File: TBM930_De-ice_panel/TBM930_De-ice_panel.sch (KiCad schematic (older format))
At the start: 77 parts, among them J1 SW_AIRFRAME_DE_ICE, J10 AVR-ISP-6, J11 Screw_Terminal_01x02, J2 SW_ICE_LIGHT, J3 SW_PROP_DE_ICE, J4 SW_WIND_SHIELD, J5 SW_PITOT_L_HTR, J6 SW_PITOT_R_HTR, J7 SW_INERT_SEP, J8 Barrel_Jack, J9 USB_B_Mini, SW1 SW_Push, SW2 SW_Push, U1 TLC5917IN, U2 TLC5917IN, U3 ATmega32U4-MU, Y1 Crystal_GND24

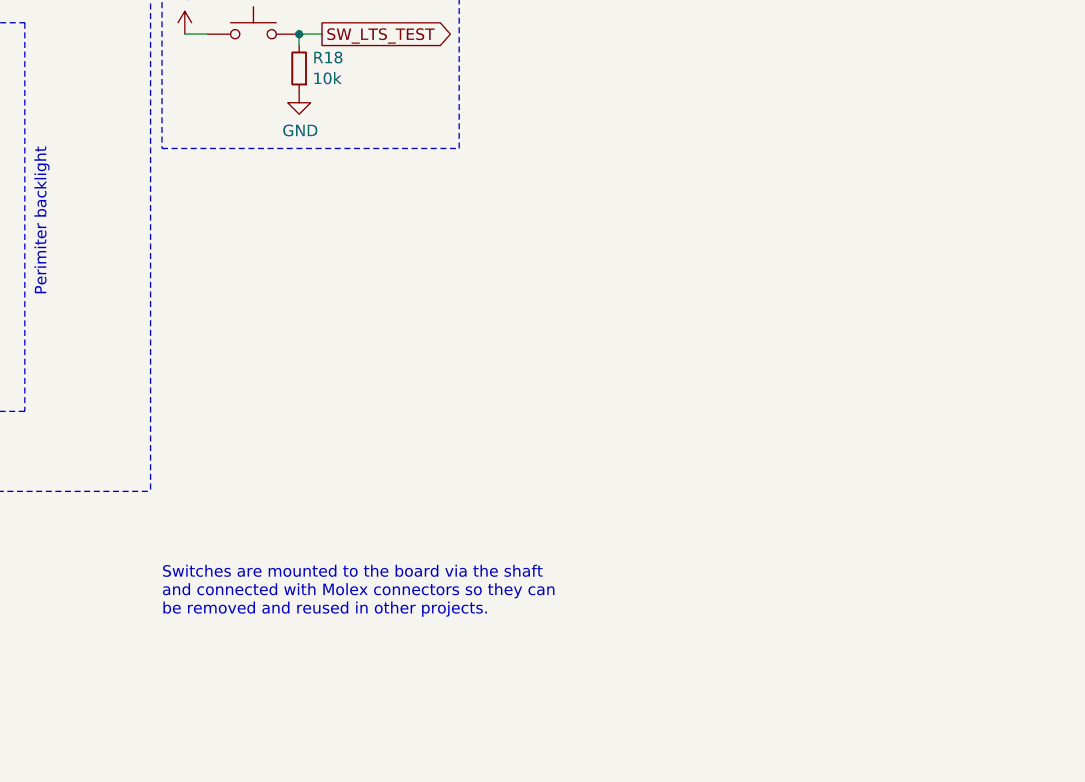
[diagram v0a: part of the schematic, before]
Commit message: Fix PCB holes
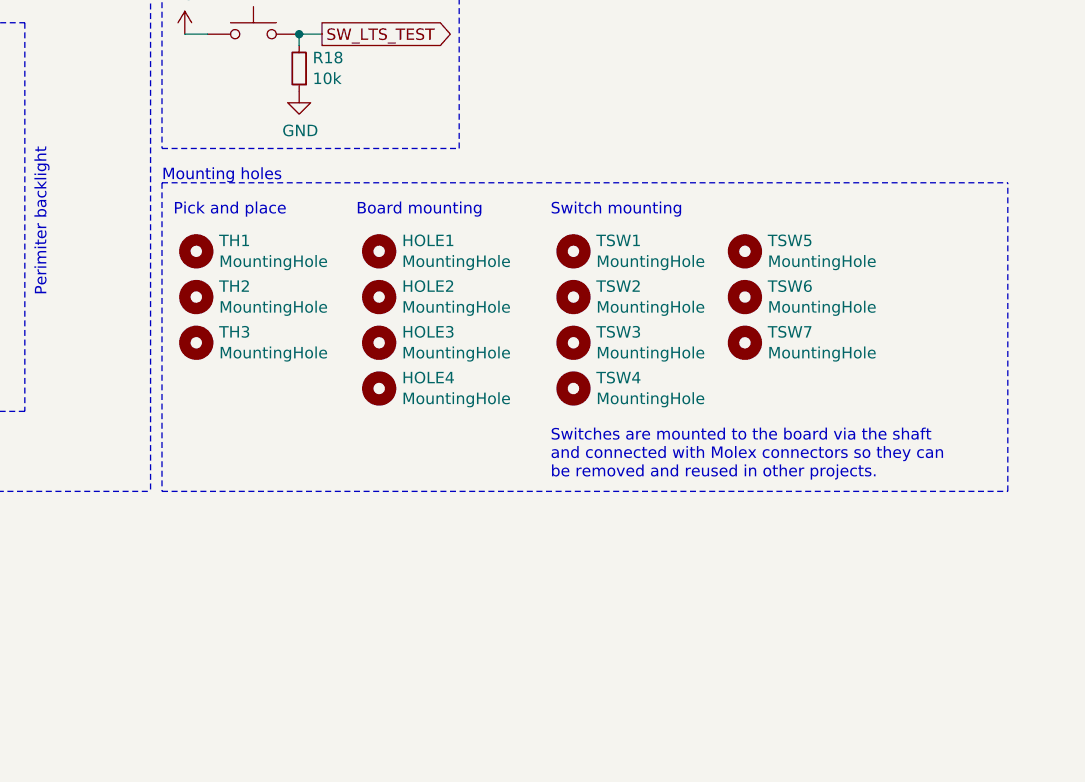
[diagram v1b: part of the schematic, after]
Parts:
- added HOLE1, HOLE2, HOLE3, HOLE4: MountingHole, MountingHole:MountingHole_3.2mm_M3, symbol Mechanical:MountingHole
- added TH1, TH2, TH3: MountingHole, TBM930 - De-ice panel:JLCPCB_Tooling_Hole, symbol Mechanical:MountingHole
- added TSW1, TSW2, TSW3, TSW4, TSW5, TSW6, TSW7: MountingHole, TBM930 - De-ice panel:MiniToggleSPDT_screw_mount, symbol Mechanical:MountingHole
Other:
- note added: "Board mounting"
- note added: "Mounting holes"
- note added: "Pick and place"
- note added: "Switch mounting"
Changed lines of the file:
@@
 	1    0    0    -1
 $EndComp
-Text Notes 9150 6350 0    50   ~ 0
+Text Notes 10850 5750 0    50   ~ 0
 Switches are mounted to the board via the shaft\nand connected with Molex connectors so they can\nbe removed and reused in other projects.\n
 Text GLabel 7000 2450 0    50   Input ~ 0
@@
 F 1 "AVR-ISP-6" H 3521 6855 50  0000 R CNN
 F 2 "Connector_PinHeader_2.54mm:PinHeader_2x03_P2.54mm_Vertical" V 3600 6900 50  0001 C CNN
-F 3 " ~" H 2575 6300 50  0001 C CNN
+F 3 "~" H 2575 6300 50  0001 C CNN
 	1    3850 6850
 	1    0    0    -1
@@
 	-1   0    0    1
 $EndComp
+$Comp
+L Mechanical:MountingHole TH1
+U 1 1 61445600
+P 9300 4750
+F 0 "TH1" H 9400 4796 50  0000 L CNN
+F 1 "MountingHole" H 9400 4705 50  0000 L CNN
+F 2 "TBM930 - De-ice panel:JLCPCB_Tooling_Hole" H 9300 4750 50  0001 C CNN
+F 3 "~" H 9300 4750 50  0001 C CNN
+	1    9300 4750
+	1    0    0    -1
+$EndComp
+$Comp
+L Mechanical:MountingHole TH2
+U 1 1 61446718
+P 9300 4950
+F 0 "TH2" H 9400 4996 50  0000 L CNN
+F 1 "MountingHole" H 9400 4905 50  0000 L CNN
+F 2 "TBM930 - De-ice panel:JLCPCB_Tooling_Hole" H 9300 4950 50  0001 C CNN
+F 3 "~" H 9300 4950 50  0001 C CNN
+	1    9300 4950
+	1    0    0    -1
+$EndComp
+$Comp
+L Mechanical:MountingHole TH3
+U 1 1 6145058F
+P 9300 5150
+F 0 "TH3" H 9400 5196 50  0000 L CNN
+F 1 "MountingHole" H 9400 5105 50  0000 L CNN
+F 2 "TBM930 - De-ice panel:JLCPCB_Tooling_Hole" H 9300 5150 50  0001 C CNN
+F 3 "~" H 9300 5150 50  0001 C CNN
+	1    9300 5150
+	1    0    0    -1
+$EndComp
+$Comp
+L Mechanical:MountingHole HOLE1
+U 1 1 6145AC3B
+P 10100 4750
+F 0 "HOLE1" H 10200 4796 50  0000 L CNN
+F 1 "MountingHole" H 10200 4705 50  0000 L CNN
+F 2 "MountingHole:MountingHole_3.2mm_M3" H 10100 4750 50  0001 C CNN
+F 3 "~" H 10100 4750 50  0001 C CNN
+	1    10100 4750
+	1    0    0    -1
+$EndComp
+$Comp
+L Mechanical:MountingHole HOLE2
+U 1 1 6146567E
+P 10100 4950
+F 0 "HOLE2" H 10200 4996 50  0000 L CNN
+F 1 "MountingHole" H 10200 4905 50  0000 L CNN
+F 2 "MountingHole:MountingHole_3.2mm_M3" H 10100 4950 50  0001 C CNN
+F 3 "~" H 10100 4950 50  0001 C CNN
+	1    10100 4950
+	1    0    0    -1
+$EndComp
+$Comp
+L Mechanical:MountingHole HOLE3
+U 1 1 6146F39B
+P 10100 5150
+F 0 "HOLE3" H 10200 5196 50  0000 L CNN
+F 1 "MountingHole" H 10200 5105 50  0000 L CNN
+F 2 "MountingHole:MountingHole_3.2mm_M3" H 10100 5150 50  0001 C CNN
+F 3 "~" H 10100 5150 50  0001 C CNN
+	1    10100 5150
+	1    0    0    -1
+$EndComp
+$Comp
+L Mechanical:MountingHole HOLE4
+U 1 1 614794E2
+P 10100 5350
+F 0 "HOLE4" H 10200 5396 50  0000 L CNN
+F 1 "MountingHole" H 10200 5305 50  0000 L CNN
+F 2 "MountingHole:MountingHole_3.2mm_M3" H 10100 5350 50  0001 C CNN
+F 3 "~" H 10100 5350 50  0001 C CNN
+	1    10100 5350
+	1    0    0    -1
+$EndComp
+$Comp
+L Mechanical:MountingHole TSW1
+U 1 1 61491315
+P 10950 4750
+F 0 "TSW1" H 11050 4796 50  0000 L CNN
+F 1 "MountingHole" H 11050 4705 50  0000 L CNN
+F 2 "TBM930 - De-ice panel:MiniToggleSPDT_screw_mount" H 10950 4750 50  0001 C CNN
+F 3 "~" H 10950 4750 50  0001 C CNN
+	1    10950 4750
+	1    0    0    -1
+$EndComp
+$Comp
+L Mechanical:MountingHole TSW2
+U 1 1 6149AD01
+P 10950 4950
+F 0 "TSW2" H 11050 4996 50  0000 L CNN
+F 1 "MountingHole" H 11050 4905 50  0000 L CNN
+F 2 "TBM930 - De-ice panel:MiniToggleSPDT_screw_mount" H 10950 4950 50  0001 C CNN
+F 3 "~" H 10950 4950 50  0001 C CNN
+	1    10950 4950
+	1    0    0    -1
+$EndComp
+$Comp
+L Mechanical:MountingHole TSW3
+U 1 1 614A4147
+P 10950 5150
+F 0 "TSW3" H 11050 5196 50  0000 L CNN
+F 1 "MountingHole" H 11050 5105 50  0000 L CNN
+F 2 "TBM930 - De-ice panel:MiniToggleSPDT_screw_mount" H 10950 5150 50  0001 C CNN
+F 3 "~" H 10950 5150 50  0001 C CNN
+	1    10950 5150
+	1    0    0    -1
+$EndComp
+$Comp
+L Mechanical:MountingHole TSW4
+U 1 1 614AD526
+P 10950 5350
+F 0 "TSW4" H 11050 5396 50  0000 L CNN
+F 1 "MountingHole" H 11050 5305 50  0000 L CNN
+F 2 "TBM930 - De-ice panel:MiniToggleSPDT_screw_mount" H 10950 5350 50  0001 C CNN
+F 3 "~" H 10950 5350 50  0001 C CNN
+	1    10950 5350
+	1    0    0    -1
+$EndComp
+$Comp
+L Mechanical:MountingHole TSW5
+U 1 1 614B67D6
+P 11700 4750
+F 0 "TSW5" H 11800 4796 50  0000 L CNN
+F 1 "MountingHole" H 11800 4705 50  0000 L CNN
+F 2 "TBM930 - De-ice panel:MiniToggleSPDT_screw_mount" H 11700 4750 50  0001 C CNN
+F 3 "~" H 11700 4750 50  0001 C CNN
+	1    11700 4750
+	1    0    0    -1
+$EndComp
+$Comp
+L Mechanical:MountingHole TSW6
+U 1 1 614BFB8D
+P 11700 4950
+F 0 "TSW6" H 11800 4996 50  0000 L CNN
+F 1 "MountingHole" H 11800 4905 50  0000 L CNN
+F 2 "TBM930 - De-ice panel:MiniToggleSPDT_screw_mount" H 11700 4950 50  0001 C CNN
+F 3 "~" H 11700 4950 50  0001 C CNN
+	1    11700 4950
+	1    0    0    -1
+$EndComp
+$Comp
+L Mechanical:MountingHole TSW7
+U 1 1 614C8F70
+P 11700 5150
+F 0 "TSW7" H 11800 5196 50  0000 L CNN
+F 1 "MountingHole" H 11800 5105 50  0000 L CNN
+F 2 "TBM930 - De-ice panel:MiniToggleSPDT_screw_mount" H 11700 5150 50  0001 C CNN
+F 3 "~" H 11700 5150 50  0001 C CNN
+	1    11700 5150
+	1    0    0    -1
+$EndComp
+Text Notes 9200 4600 0    50   ~ 0
+Pick and place
+Text Notes 10000 4600 0    50   ~ 0
+Board mounting
+Text Notes 10850 4600 0    50   ~ 0
+Switch mounting
+Wire Notes Line
+	9150 4450 9150 5800
+Wire Notes Line
+	9150 5800 12850 5800
+Wire Notes Line
+	12850 5800 12850 4450
+Wire Notes Line
+	9150 4450 12850 4450
+Text Notes 9150 4450 0    50   ~ 0
+Mounting holes
 $EndSCHEMATC
